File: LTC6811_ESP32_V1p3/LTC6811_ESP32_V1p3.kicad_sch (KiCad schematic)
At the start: 18 parts, among them J10 Hole /NC, J11 Hole /NC, J12 Hole /NC, J2 OLED /NC, J31 CAN /NC, J4 USB, J9 Hole /NC, Q1 BSS138

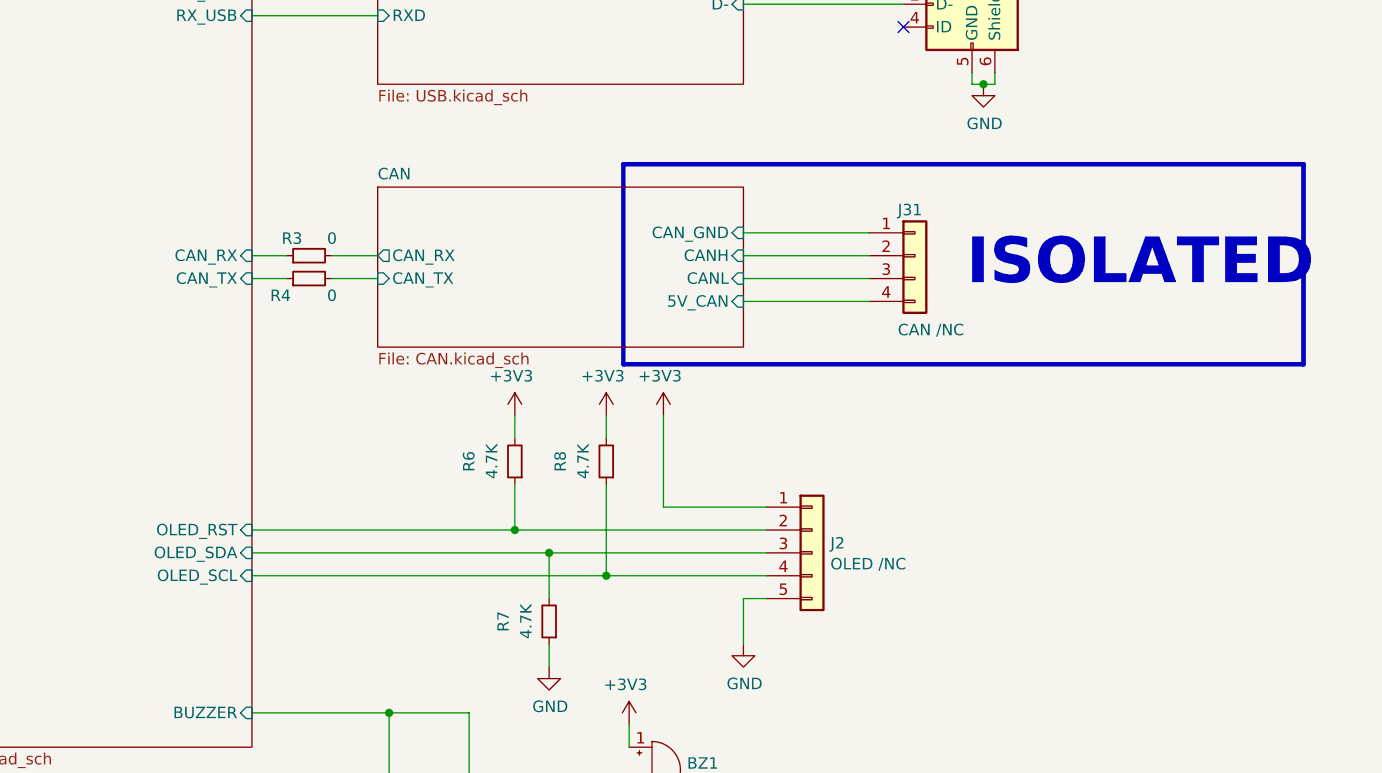
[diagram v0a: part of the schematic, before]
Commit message: Optimize signal transmission lines.
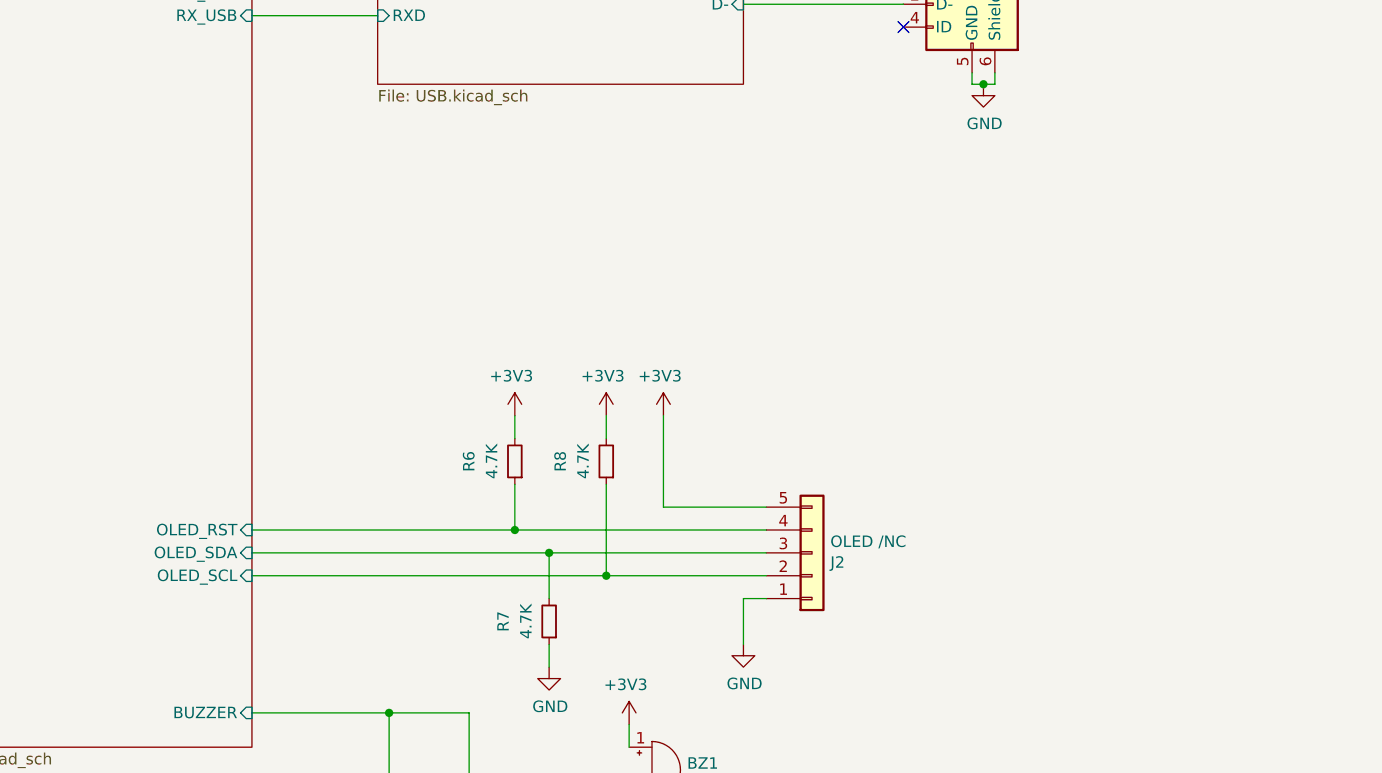
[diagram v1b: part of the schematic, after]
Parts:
- removed J31: CAN /NC, Connector_PinHeader_2.54mm:PinHeader_1x04_P2.54mm_Vertical, symbol Connector_Generic:Conn_01x04
- removed R3, R4: 0, Resistor_SMD:R_0603_1608Metric, symbol Device:R_Small
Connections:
- net +3V3: now also J2.5 (Pin_5); no longer J2.1 (Pin_1)
- net GND: now also J2.1 (Pin_1); no longer J2.5 (Pin_5)
- net MCU/OLED_RST: now also J2.4 (Pin_4); no longer J2.2 (Pin_2)
- net MCU/OLED_SCL: now also J2.2 (Pin_2); no longer J2.4 (Pin_4)
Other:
- removed sheet CAN
- sheet MCU ports: added none; removed CAN_RX, CAN_TX
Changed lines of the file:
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@@
-    (stroke (width 0) (type default))
-  )
-  (wire (pts (xy 227.965 125.73) (xy 231.775 125.73))
     (stroke (width 0) (type default))
   )
@@
     (stroke (width 0) (type default))
   )
-  (wire (pts (xy 296.545 125.73) (xy 282.575 125.73))
-    (stroke (width 0) (type default))
-  )
   (wire (pts (xy 282.575 161.29) (xy 282.575 166.37))
     (stroke (width 0) (type default))
@@
     (stroke (width 0) (type default))
   )
-  (wire (pts (xy 282.575 123.19) (xy 296.545 123.19))
-    (stroke (width 0) (type default))
-  )
   (wire (pts (xy 174.625 85.725) (xy 174.625 111.76))
     (stroke (width 0) (type default))
@@
     (stroke (width 0) (type default))
   )
-  (wire (pts (xy 227.965 123.19) (xy 231.775 123.19))
-    (stroke (width 0) (type default))
-  )
   (wire (pts (xy 310.515 104.14) (xy 310.515 102.87))
     (stroke (width 0) (type default))
@@
     (stroke (width 0) (type default))
   )
-  (wire (pts (xy 236.855 125.73) (xy 241.935 125.73))
-    (stroke (width 0) (type default))
-  )
   (wire (pts (xy 179.705 185.42) (xy 179.705 189.23))
     (stroke (width 0) (type default))
@@
     (stroke (width 0) (type default))
   )
-  (wire (pts (xy 296.545 120.65) (xy 282.575 120.65))
-    (stroke (width 0) (type default))
-  )
   (wire (pts (xy 227.965 156.21) (xy 260.985 156.21))
     (stroke (width 0) (type default))
@@
   )
   (wire (pts (xy 252.095 190.5) (xy 262.255 190.5))
-    (stroke (width 0) (type default))
-  )
-  (wire (pts (xy 282.575 128.27) (xy 296.545 128.27))
-    (stroke (width 0) (type default))
-  )
-  (wire (pts (xy 236.855 123.19) (xy 241.935 123.19))
     (stroke (width 0) (type default))
   )
@@
     (fill (type none))
   )
-  (rectangle (start 269.24 113.03) (end 344.805 135.255)
-    (stroke (width 0.5) (type default))
-    (fill (type none))
-  )
   (rectangle (start 152.4 59.69) (end 152.4 59.69)
     (stroke (width 0) (type default))
@@
   )
   (text "ISOLATED" (at 73.66 145.415 0)
-    (effects (font (size 5.08 5.08) (thickness 1.016) bold) (justify left bottom))
-  )
-  (text "ISOLATED" (at 307.34 127 0)
     (effects (font (size 5.08 5.08) (thickness 1.016) bold) (justify left bottom))
   )
@@
     )
   )
-  (symbol (lib_id "Connector_Generic:Conn_01x05") (at 290.195 156.21 0) (unit 1)
-    (in_bom yes) (on_board yes) (dnp no)
-    (property "Reference" "J2" (at 292.227 155.1432 0)
+  (symbol (lib_id "Connector_Generic:Conn_01x05") (at 290.195 156.21 0) (mirror x) (unit 1)
+    (in_bom yes) (on_board yes) (dnp no)
+    (property "Reference" "J2" (at 292.227 157.2768 0)
       (effects (font (size 1.27 1.27)) (justify left))
     )
-    (property "Value" "OLED /NC" (at 292.227 157.4546 0)
+    (property "Value" "OLED /NC" (at 292.227 154.9654 0)
       (effects (font (size 1.27 1.27)) (justify left))
     )
@@
     )
   )
-  (symbol (lib_id "Device:R_Small") (at 234.315 125.73 90) (unit 1)
-    (in_bom yes) (on_board yes) (dnp no)
-    (property "Reference" "R4" (at 231.14 127.635 90)
-      (effects (font (size 1.27 1.27)))
-    )
-    (property "Value" "0" (at 236.855 127.635 90)
-      (effects (font (size 1.27 1.27)))
-    )
-    (property "Footprint" "Resistor_SMD:R_0603_1608Metric" (at 234.315 125.73 0)
-      (effects (font (size 1.27 1.27)) hide)
-    )
-    (property "Datasheet" "https://www.yageo.com/upload/media/product/products/datasheet/rchip/PYu-RC_Group_51_RoHS_L_12.pdf" (at 234.315 125.73 0)
-      (effects (font (size 1.27 1.27)) hide)
-    )
-    (property "MPN" "RC0603JR-070RL" (at 234.315 125.73 0)
-      (effects (font (size 1.27 1.27)) hide)
-    )
-    (property "Description" "0 Ohms Jumper Chip Resistor 0603 (1608 Metric) Moisture Resistant Thick Film" (at 234.315 125.73 0)
-      (effects (font (size 1.27 1.27)) hide)
-    )
-    (property "Link" "https://www.digikey.jp/en/products/detail/yageo/RC0603JR-070RL/726675?s=N4IgTCBcDaIEoGEAMA2JBmAUnAtEg7EnADIgC6AvkA" (at 234.315 125.73 0)
-      (effects (font (size 1.27 1.27)) hide)
-    )
-    (pin "1")
-    (pin "2")
-    (instances
-      (project "LTC6811_ESP32_V1p3"
-        (path "/6a86ff6f-b159-4c4c-8a40-e732cc82e010"
-          (reference "R4") (unit 1)
-        )
-      )
-    )
-  )
   (symbol (lib_id "power:+3V3") (at 257.175 140.97 0) (mirror y) (unit 1)
     (in_bom yes) (on_board yes) (dnp no)
@@
     )
   )
-  (symbol (lib_id "Connector_Generic:Conn_01x04") (at 301.625 123.19 0) (unit 1)
-    (in_bom yes) (on_board yes) (dnp no)
-    (property "Reference" "J31" (at 299.72 118.11 0)
-      (effects (font (size 1.27 1.27)) (justify left))
-    )
-    (property "Value" "CAN /NC" (at 299.72 131.445 0)
-      (effects (font (size 1.27 1.27)) (justify left))
-    )
-    (property "Footprint" "Connector_PinHeader_2.54mm:PinHeader_1x04_P2.54mm_Vertical" (at 301.625 123.19 0)
-      (effects (font (size 1.27 1.27)) hide)
-    )
-    (property "Datasheet" "https://cdn.amphenol-cs.com/media/wysiwyg/files/drawing/g800wxxxxxxeu_1.pdf" (at 301.625 123.19 0)
-      (effects (font (size 1.27 1.27)) hide)
-    )
-    (property "Description" "Connector Header Through Hole 4 position 0.100\" (2.54mm)" (at 301.625 123.19 0)
-      (effects (font (size 1.27 1.27)) hide)
-    )
-    (property "Link" "https://www.digikey.jp/en/products/detail/amphenol-cs-commercial-products/G800W304018EU/13682993" (at 301.625 123.19 0)
-      (effects (font (size 1.27 1.27)) hide)
-    )
-    (property "MPN" "G800W304018EU" (at 301.625 123.19 0)
-      (effects (font (size 1.27 1.27)) hide)
-    )
-    (pin "1")
-    (pin "2")
-    (pin "3")
-    (pin "4")
-    (instances
-      (project "LTC6811_ESP32_V1p3"
-        (path "/6a86ff6f-b159-4c4c-8a40-e732cc82e010/00000000-0000-0000-0000-00005ab72d4d"
-          (reference "J31") (unit 1)
-        )
-        (path "/6a86ff6f-b159-4c4c-8a40-e732cc82e010"
-          (reference "J3") (unit 1)
-        )
-      )
-      (project "L9963E+ESP32"
-        (path "/e9bba7f0-c10d-45df-9f8e-74901087917a"
-          (reference "J3") (unit 1)
-        )
-      )
-    )
-  )
-  (symbol (lib_id "Device:R_Small") (at 234.315 123.19 90) (unit 1)
-    (in_bom yes) (on_board yes) (dnp no)
-    (property "Reference" "R3" (at 232.41 121.285 90)
-      (effects (font (size 1.27 1.27)))
-    )
-    (property "Value" "0" (at 236.855 121.285 90)
-      (effects (font (size 1.27 1.27)))
-    )
-    (property "Footprint" "Resistor_SMD:R_0603_1608Metric" (at 234.315 123.19 0)
-      (effects (font (size 1.27 1.27)) hide)
-    )
-    (property "Datasheet" "https://www.yageo.com/upload/media/product/products/datasheet/rchip/PYu-RC_Group_51_RoHS_L_12.pdf" (at 234.315 123.19 0)
-      (effects (font (size 1.27 1.27)) hide)
-    )
-    (property "MPN" "RC0603JR-070RL" (at 234.315 123.19 0)
-      (effects (font (size 1.27 1.27)) hide)
-    )
-    (property "Description" "0 Ohms Jumper Chip Resistor 0603 (1608 Metric) Moisture Resistant Thick Film" (at 234.315 123.19 0)
-      (effects (font (size 1.27 1.27)) hide)
-    )
-    (property "Link" "https://www.digikey.jp/en/products/detail/yageo/RC0603JR-070RL/726675?s=N4IgTCBcDaIEoGEAMA2JBmAUnAtEg7EnADIgC6AvkA" (at 234.315 123.19 0)
-      (effects (font (size 1.27 1.27)) hide)
-    )
-    (pin "1")
-    (pin "2")
-    (instances
-      (project "LTC6811_ESP32_V1p3"
-        (path "/6a86ff6f-b159-4c4c-8a40-e732cc82e010"
-          (reference "R3") (unit 1)
-        )
-      )
-    )
-  )
   (symbol (lib_id "power:+3V3") (at 267.335 140.97 0) (mirror y) (unit 1)
     (in_bom yes) (on_board yes) (dnp no)
@@
           (reference "LOGO1") (unit 1)
         )
-      )
-    )
-  )
-  (sheet (at 241.935 115.57) (size 40.64 17.78) (fields_autoplaced)
-    (stroke (width 0) (type solid))
-    (fill (color 0 0 0 0.0000))
-    (property "Sheetname" "CAN" (at 241.935 114.8584 0)
-      (effects (font (size 1.27 1.27)) (justify left bottom))
-    )
-    (property "Sheetfile" "CAN.kicad_sch" (at 241.935 133.9346 0)
-      (effects (font (size 1.27 1.27)) (justify left top))
-    )
-    (pin "CAN_RX" output (at 241.935 123.19 180)
-      (effects (font (size 1.27 1.27)) (justify left))
-    )
-    (pin "CAN_TX" input (at 241.935 125.73 180)
-      (effects (font (size 1.27 1.27)) (justify left))
-    )
-    (pin "CANH" input (at 282.575 123.19 0)
-      (effects (font (size 1.27 1.27)) (justify right))
-    )
-    (pin "CANL" input (at 282.575 125.73 0)
-      (effects (font (size 1.27 1.27)) (justify right))
-    )
-    (pin "5V_CAN" input (at 282.575 128.27 0)
-      (effects (font (size 1.27 1.27)) (justify right))
-    )
-    (pin "CAN_GND" input (at 282.575 120.65 0)
-      (effects (font (size 1.27 1.27)) (justify right))
-    )
-    (instances
-      (project "LTC6811_ESP32_V1p3"
-        (path "/6a86ff6f-b159-4c4c-8a40-e732cc82e010" (page "6"))
       )
     )
@@
       (effects (font (size 1.27 1.27)) (justify left))
     )
-    (pin "CAN_RX" input (at 227.965 123.19 0)
-      (effects (font (size 1.27 1.27)) (justify right))
-    )
-    (pin "CAN_TX" input (at 227.965 125.73 0)
-      (effects (font (size 1.27 1.27)) (justify right))
-    )
     (pin "BUZZER" input (at 227.965 173.99 0)

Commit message: Add files via upload
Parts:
- renumbered LOGO2 to LOGO1
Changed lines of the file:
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@@
       (effects (font (size 1.27 1.27)) hide)
     )
-    (property "Datasheet" "~" (at 304.165 93.98 0)
+    (property "Datasheet" "chrome-extension://efaidnbmnnnibpcajpcglclefindmkaj/https://www.te.com/usa-en/product-2013499-1.datasheet.pdf" (at 304.165 93.98 0)
       (effects (font (size 1.27 1.27)) hide)
     )
@@
     (instances
       (project "LTC6811_ESP32_V1p3"
-        (path "/6a86ff6f-b159-4c4c-8a40-e732cc82e010/0999518d-09c3-4a69-bd78-ff81b3ce8dd2"
-          (reference "J9") (unit 1)
-        )
         (path "/6a86ff6f-b159-4c4c-8a40-e732cc82e010"
           (reference "J9") (unit 1)
@@
   (symbol (lib_id "power:+3V3") (at 269.875 175.26 0) (mirror y) (unit 1)
     (in_bom yes) (on_board yes) (dnp no)
-    (property "Reference" "#PWR022" (at 269.875 179.07 0)
+    (property "Reference" "#PWR011" (at 269.875 179.07 0)
       (effects (font (size 1.27 1.27)) hide)
     )
@@
     (instances
       (project "LTC6811_ESP32_V1p3"
-        (path "/6a86ff6f-b159-4c4c-8a40-e732cc82e010/00000000-0000-0000-0000-00005c519ba0"
-          (reference "#PWR022") (unit 1)
-        )
-        (path "/6a86ff6f-b159-4c4c-8a40-e732cc82e010/00000000-0000-0000-0000-00005ac18063"
-          (reference "#PWR022") (unit 1)
-        )
         (path "/6a86ff6f-b159-4c4c-8a40-e732cc82e010"
           (reference "#PWR011") (unit 1)
@@
   (symbol (lib_id "power:+3V3") (at 257.175 140.97 0) (mirror y) (unit 1)
     (in_bom yes) (on_board yes) (dnp no)
-    (property "Reference" "#PWR022" (at 257.175 144.78 0)
+    (property "Reference" "#PWR013" (at 257.175 144.78 0)
       (effects (font (size 1.27 1.27)) hide)
     )
@@
     (instances
       (project "LTC6811_ESP32_V1p3"
-        (path "/6a86ff6f-b159-4c4c-8a40-e732cc82e010/00000000-0000-0000-0000-00005c519ba0"
-          (reference "#PWR022") (unit 1)
-        )
-        (path "/6a86ff6f-b159-4c4c-8a40-e732cc82e010/00000000-0000-0000-0000-00005ac18063"
-          (reference "#PWR022") (unit 1)
-        )
         (path "/6a86ff6f-b159-4c4c-8a40-e732cc82e010"
           (reference "#PWR013") (unit 1)
@@
     (instances
       (project "LTC6811_ESP32_V1p3"
-        (path "/6a86ff6f-b159-4c4c-8a40-e732cc82e010/0999518d-09c3-4a69-bd78-ff81b3ce8dd2"
-          (reference "J10") (unit 1)
-        )
         (path "/6a86ff6f-b159-4c4c-8a40-e732cc82e010"
           (reference "J10") (unit 1)
@@
     (instances
       (project "LTC6811_ESP32_V1p3"
-        (path "/6a86ff6f-b159-4c4c-8a40-e732cc82e010/0999518d-09c3-4a69-bd78-ff81b3ce8dd2"
-          (reference "J11") (unit 1)
-        )
         (path "/6a86ff6f-b159-4c4c-8a40-e732cc82e010"
           (reference "J11") (unit 1)
@@
     (instances
       (project "LTC6811_ESP32_V1p3"
-        (path "/6a86ff6f-b159-4c4c-8a40-e732cc82e010/0999518d-09c3-4a69-bd78-ff81b3ce8dd2"
-          (reference "J12") (unit 1)
-        )
         (path "/6a86ff6f-b159-4c4c-8a40-e732cc82e010"
           (reference "J12") (unit 1)
@@
   (symbol (lib_id "power:+3V3") (at 273.685 140.97 0) (mirror y) (unit 1)
     (in_bom yes) (on_board yes) (dnp no)
-    (property "Reference" "#PWR022" (at 273.685 144.78 0)
+    (property "Reference" "#PWR08" (at 273.685 144.78 0)
       (effects (font (size 1.27 1.27)) hide)
     )
@@
     (instances
       (project "LTC6811_ESP32_V1p3"
-        (path "/6a86ff6f-b159-4c4c-8a40-e732cc82e010/00000000-0000-0000-0000-00005c519ba0"
-          (reference "#PWR022") (unit 1)
-        )
-        (path "/6a86ff6f-b159-4c4c-8a40-e732cc82e010/00000000-0000-0000-0000-00005ac18063"
-          (reference "#PWR022") (unit 1)
-        )
         (path "/6a86ff6f-b159-4c4c-8a40-e732cc82e010"
           (reference "#PWR08") (unit 1)
@@
   (symbol (lib_id "power:+3V3") (at 267.335 140.97 0) (mirror y) (unit 1)
     (in_bom yes) (on_board yes) (dnp no)
-    (property "Reference" "#PWR022" (at 267.335 144.78 0)
+    (property "Reference" "#PWR010" (at 267.335 144.78 0)
       (effects (font (size 1.27 1.27)) hide)
     )
@@
     (instances
       (project "LTC6811_ESP32_V1p3"
-        (path "/6a86ff6f-b159-4c4c-8a40-e732cc82e010/00000000-0000-0000-0000-00005c519ba0"
-          (reference "#PWR022") (unit 1)
-        )
-        (path "/6a86ff6f-b159-4c4c-8a40-e732cc82e010/00000000-0000-0000-0000-00005ac18063"
-          (reference "#PWR022") (unit 1)
-        )
         (path "/6a86ff6f-b159-4c4c-8a40-e732cc82e010"
           (reference "#PWR010") (unit 1)
@@
   (symbol (lib_id "Fiber_Optic:logo") (at 330.2 260.985 0) (unit 1)
     (in_bom yes) (on_board yes) (dnp no) (fields_autoplaced)
-    (property "Reference" "LOGO2" (at 337.947 252.222 0)
+    (property "Reference" "LOGO1" (at 337.947 252.222 0)
       (effects (font (size 1.27 1.27)) hide)
     )
@@
     (instances
       (project "LTC6811_ESP32_V1p3"
-        (path "/6a86ff6f-b159-4c4c-8a40-e732cc82e010/0999518d-09c3-4a69-bd78-ff81b3ce8dd2"
-          (reference "LOGO2") (unit 1)
-        )
         (path "/6a86ff6f-b159-4c4c-8a40-e732cc82e010"
           (reference "LOGO1") (unit 1)
